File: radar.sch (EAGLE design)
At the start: 9 parts, among them J1 APP_2POS_CONFIG12V_HORIZ, U1 OKI-78SR-3.3/1.5-W36HC, U2 OKI-78SR-5/1.5-W36HC

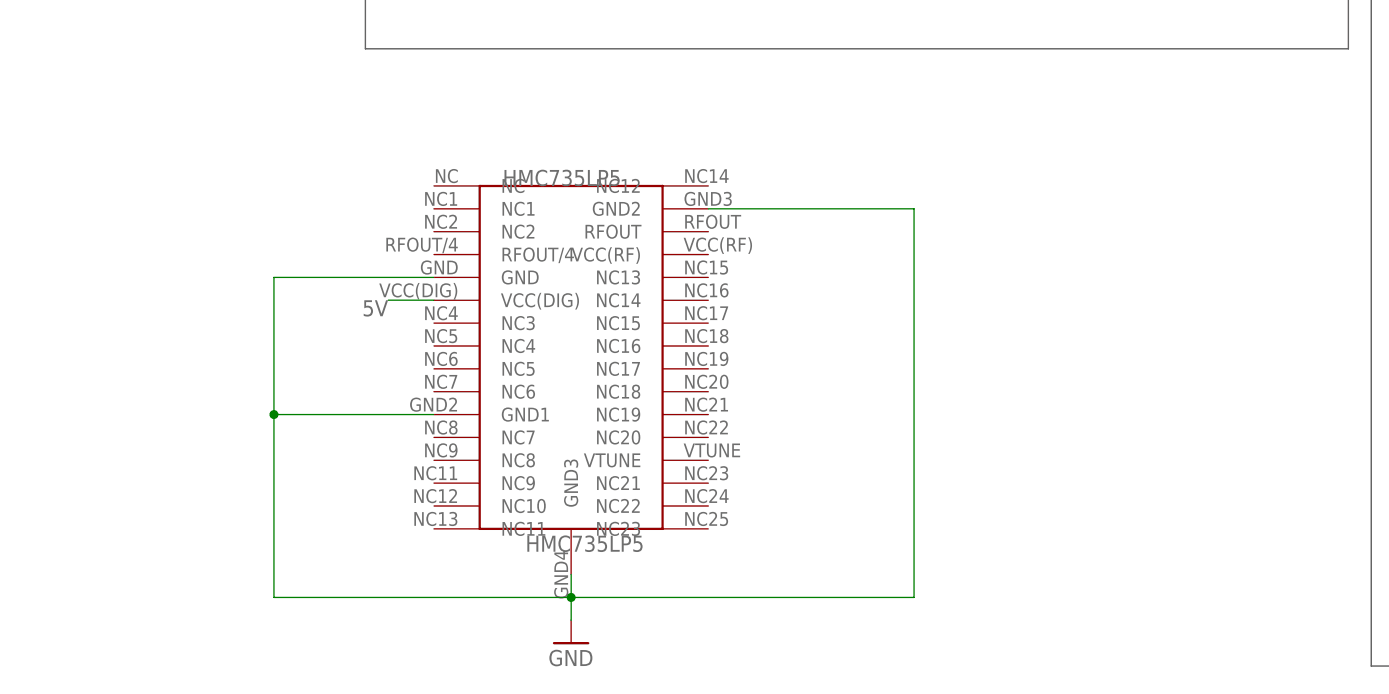
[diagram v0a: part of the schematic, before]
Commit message: Created PLL library and added it to schematic
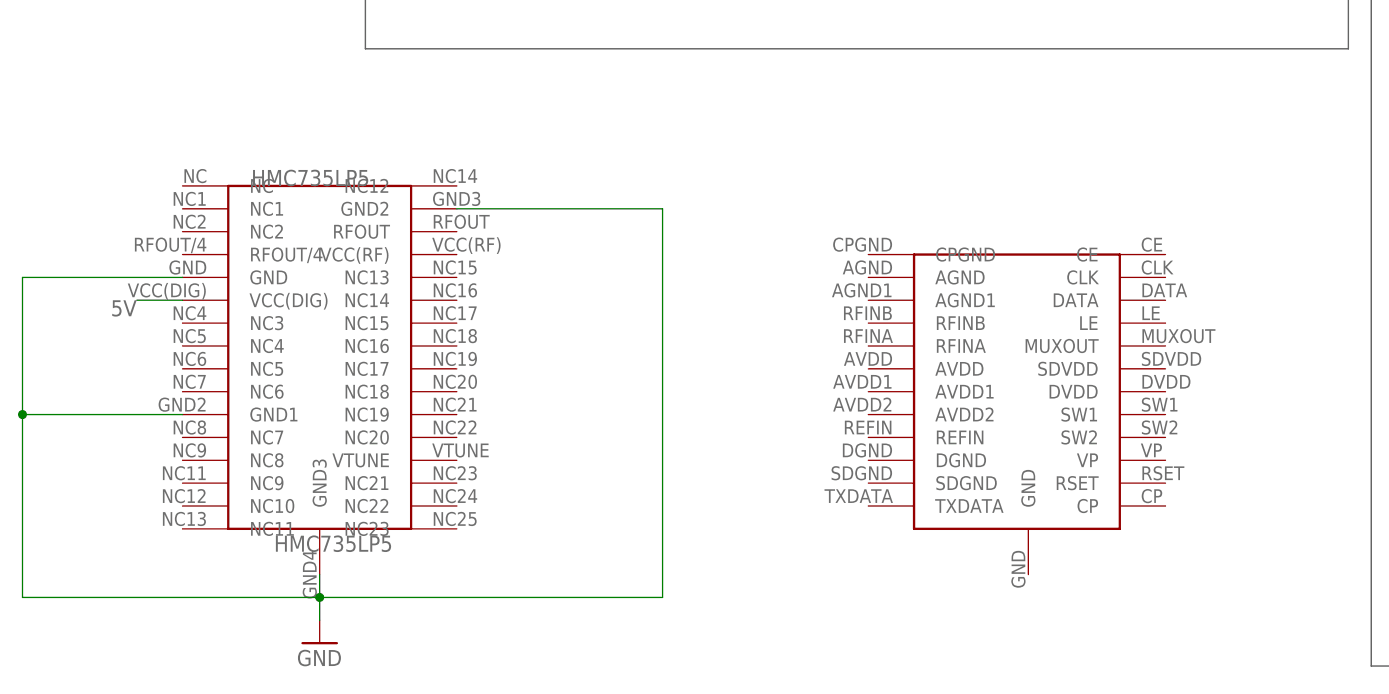
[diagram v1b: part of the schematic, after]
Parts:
- added U$3: ADF4169, ADF4169:ADF4169
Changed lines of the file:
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@@
 <part name="GND4" library="supply1" deviceset="GND" device=""/>
 <part name="U$2" library="HMC735LP5" deviceset="HMC735LP5" device=""/>
+<part name="U$3" library="ADF4169" deviceset="ADF4169" device=""/>
 </parts>
 <sheets>
@@
 <instance part="GND2" gate="1" x="0" y="109.22"/>
 <instance part="GND3" gate="1" x="43.18" y="109.22"/>
-<instance part="GND4" gate="1" x="-2.54" y="30.48"/>
-<instance part="U$2" gate="G$1" x="-2.54" y="68.58"/>
+<instance part="GND4" gate="1" x="-30.48" y="30.48"/>
+<instance part="U$2" gate="G$1" x="-30.48" y="68.58"/>
+<instance part="U$3" gate="G$1" x="45.72" y="55.88"/>
 </instances>
 <busses>
@@
 <pinref part="GND4" gate="1" pin="GND"/>
 <pinref part="U$2" gate="G$1" pin="GND3"/>
-<wire x1="-2.54" y1="33.02" x2="-2.54" y2="35.56" width="0.1524" layer="91"/>
+<wire x1="-30.48" y1="33.02" x2="-30.48" y2="35.56" width="0.1524" layer="91"/>
 <pinref part="U$2" gate="G$1" pin="GND"/>
-<wire x1="-2.54" y1="35.56" x2="-2.54" y2="38.1" width="0.1524" layer="91"/>
-<wire x1="-17.78" y1="71.12" x2="-35.56" y2="71.12" width="0.1524" layer="91"/>
-<wire x1="-35.56" y1="71.12" x2="-35.56" y2="55.88" width="0.1524" layer="91"/>
-<wire x1="-35.56" y1="55.88" x2="-35.56" y2="35.56" width="0.1524" layer="91"/>
-<wire x1="-35.56" y1="35.56" x2="-2.54" y2="35.56" width="0.1524" layer="91"/>
-<junction x="-2.54" y="35.56"/>
+<wire x1="-30.48" y1="35.56" x2="-30.48" y2="38.1" width="0.1524" layer="91"/>
+<wire x1="-45.72" y1="71.12" x2="-63.5" y2="71.12" width="0.1524" layer="91"/>
+<wire x1="-63.5" y1="71.12" x2="-63.5" y2="55.88" width="0.1524" layer="91"/>
+<wire x1="-63.5" y1="55.88" x2="-63.5" y2="35.56" width="0.1524" layer="91"/>
+<wire x1="-63.5" y1="35.56" x2="-30.48" y2="35.56" width="0.1524" layer="91"/>
+<junction x="-30.48" y="35.56"/>
 <pinref part="U$2" gate="G$1" pin="GND1"/>
-<wire x1="-17.78" y1="55.88" x2="-35.56" y2="55.88" width="0.1524" layer="91"/>
-<junction x="-35.56" y="55.88"/>
+<wire x1="-45.72" y1="55.88" x2="-63.5" y2="55.88" width="0.1524" layer="91"/>
+<junction x="-63.5" y="55.88"/>
 <pinref part="U$2" gate="G$1" pin="GND2"/>
-<wire x1="12.7" y1="78.74" x2="35.56" y2="78.74" width="0.1524" layer="91"/>
-<wire x1="35.56" y1="78.74" x2="35.56" y2="35.56" width="0.1524" layer="91"/>
-<wire x1="35.56" y1="35.56" x2="-2.54" y2="35.56" width="0.1524" layer="91"/>
+<wire x1="-15.24" y1="78.74" x2="7.62" y2="78.74" width="0.1524" layer="91"/>
+<wire x1="7.62" y1="78.74" x2="7.62" y2="35.56" width="0.1524" layer="91"/>
+<wire x1="7.62" y1="35.56" x2="-30.48" y2="35.56" width="0.1524" layer="91"/>
 </segment>
 </net>
@@
 <segment>
 <pinref part="U$2" gate="G$1" pin="VCC(DIG)"/>
-<wire x1="-17.78" y1="68.58" x2="-22.86" y2="68.58" width="0.1524" layer="91"/>
-<label x="-22.86" y="68.58" size="1.778" layer="95" rot="R180"/>
+<wire x1="-45.72" y1="68.58" x2="-50.8" y2="68.58" width="0.1524" layer="91"/>
+<label x="-50.8" y="68.58" size="1.778" layer="95" rot="R180"/>
 </segment>
 </net>

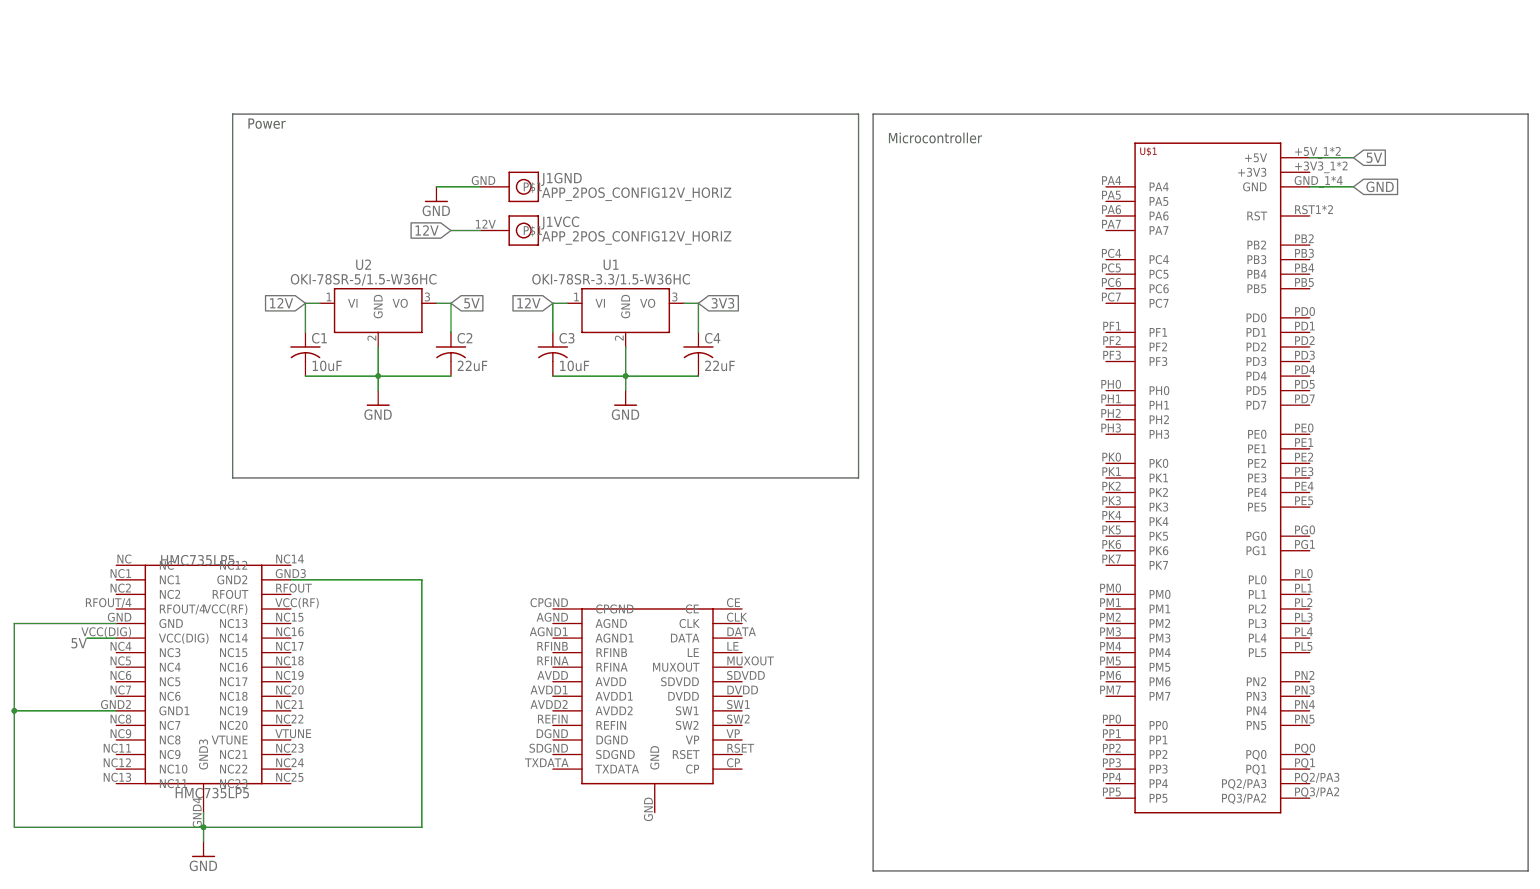
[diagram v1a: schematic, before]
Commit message: Started board layout
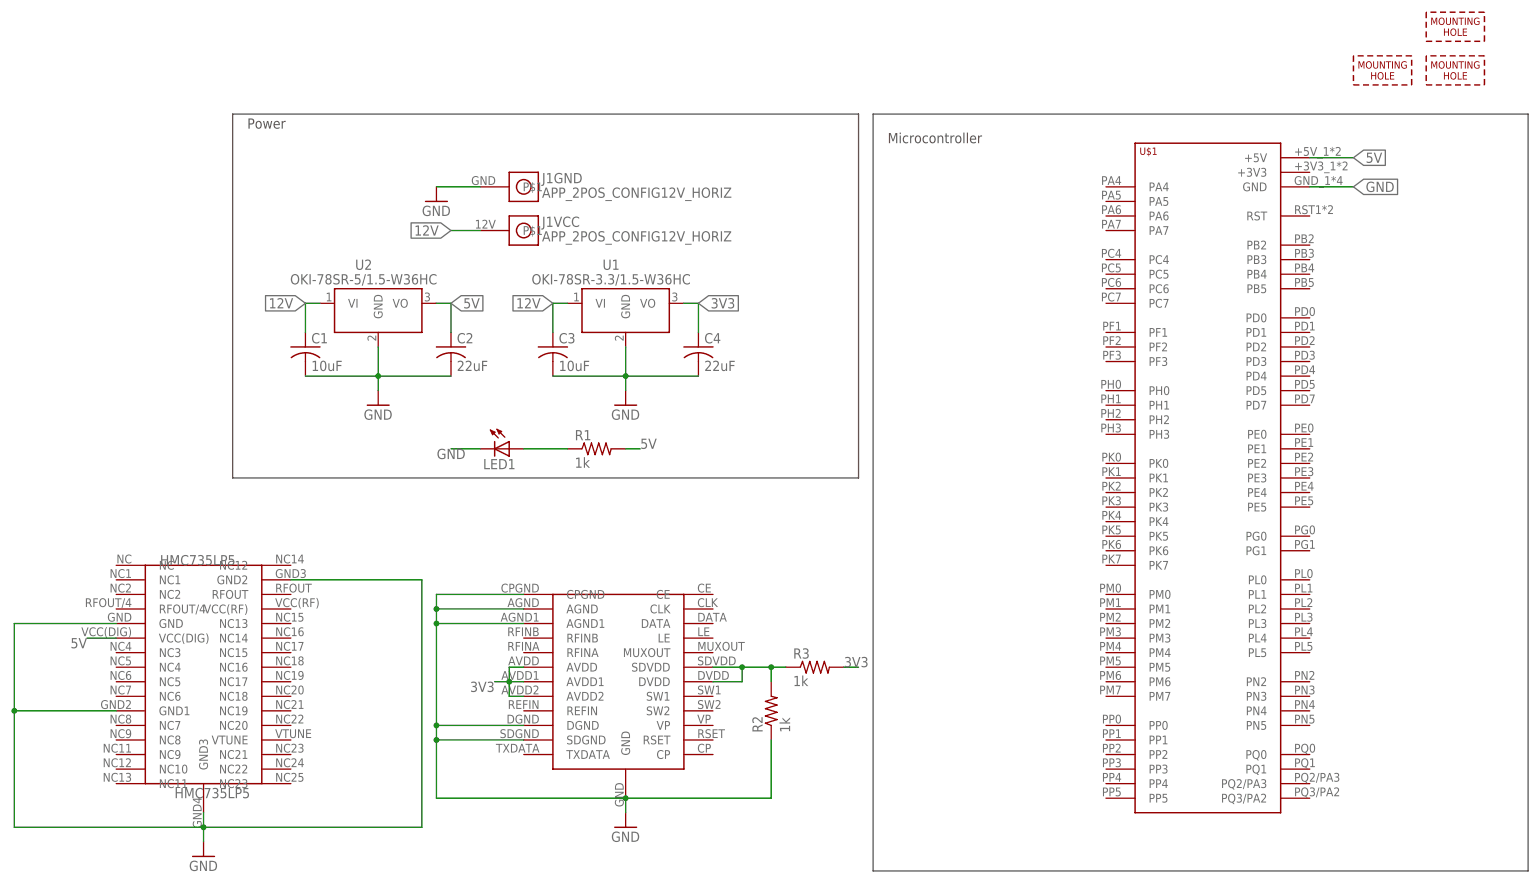
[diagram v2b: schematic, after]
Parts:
- added H1, H2, H3: MOUNTING_HOLE#6, MRDT-Hardware:MOUNTING_HOLE#6
- added LED1: (no value), led:LEDCHIP-LED0805
- added R1, R2, R3: 1k, rcl:R-US_M0805
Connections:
- new net N$1: LED1.A, R1.1
- new net N$2: R2.2, R3.1, U$3.DVDD, U$3.SDVDD
- net 3V3: now also R3.2, U$3.AVDD, U$3.AVDD1, U$3.AVDD2
- net 5V: now also R1.2
- net GND: now also LED1.C, R2.1, U$3.AGND, U$3.AGND1, U$3.CPGND, U$3.DGND, U$3.GND, U$3.SDGND
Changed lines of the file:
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@@
 <part name="U$2" library="HMC735LP5" deviceset="HMC735LP5" device=""/>
 <part name="U$3" library="ADF4169" deviceset="ADF4169" device=""/>
+<part name="LED1" library="led" deviceset="LED" device="CHIP-LED0805"/>
+<part name="R1" library="rcl" deviceset="R-US_" device="M0805" value="1k"/>
+<part name="GND5" library="supply1" deviceset="GND" device=""/>
+<part name="R2" library="rcl" deviceset="R-US_" device="M0805" value="1k"/>
+<part name="R3" library="rcl" deviceset="R-US_" device="M0805" value="1k"/>
+<part name="H1" library="MRDT-Hardware" deviceset="MOUNTING_HOLE" device="#6"/>
+<part name="H2" library="MRDT-Hardware" deviceset="MOUNTING_HOLE" device="#6"/>
+<part name="H3" library="MRDT-Hardware" deviceset="MOUNTING_HOLE" device="#6"/>
 </parts>
 <sheets>
@@
 <instance part="GND4" gate="1" x="-30.48" y="30.48"/>
 <instance part="U$2" gate="G$1" x="-30.48" y="68.58"/>
-<instance part="U$3" gate="G$1" x="45.72" y="55.88"/>
+<instance part="U$3" gate="G$1" x="40.64" y="58.42"/>
+<instance part="LED1" gate="G$1" x="22.86" y="101.6" rot="R270"/>
+<instance part="R1" gate="G$1" x="38.1" y="101.6"/>
+<instance part="GND5" gate="1" x="43.18" y="35.56"/>
+<instance part="R2" gate="G$1" x="68.58" y="55.88" rot="R90"/>
+<instance part="R3" gate="G$1" x="76.2" y="63.5"/>
+<instance part="H1" gate="G$1" x="182.88" y="165.1"/>
+<instance part="H2" gate="G$1" x="182.88" y="172.72"/>
+<instance part="H3" gate="G$1" x="170.18" y="165.1"/>
 </instances>
 <busses>
@@
 <wire x1="7.62" y1="35.56" x2="-30.48" y2="35.56" width="0.1524" layer="91"/>
 </segment>
+<segment>
+<pinref part="LED1" gate="G$1" pin="C"/>
+<wire x1="17.78" y1="101.6" x2="12.7" y2="101.6" width="0.1524" layer="91"/>
+<label x="15.24" y="101.6" size="1.778" layer="95" rot="R180"/>
+</segment>
+<segment>
+<pinref part="U$3" gate="G$1" pin="CPGND"/>
+<wire x1="25.4" y1="76.2" x2="10.16" y2="76.2" width="0.1524" layer="91"/>
+<wire x1="10.16" y1="76.2" x2="10.16" y2="73.66" width="0.1524" layer="91"/>
+<pinref part="U$3" gate="G$1" pin="GND"/>
+<wire x1="10.16" y1="73.66" x2="10.16" y2="71.12" width="0.1524" layer="91"/>
+<wire x1="10.16" y1="71.12" x2="10.16" y2="53.34" width="0.1524" layer="91"/>
+<wire x1="10.16" y1="53.34" x2="10.16" y2="50.8" width="0.1524" layer="91"/>
+<wire x1="10.16" y1="50.8" x2="10.16" y2="40.64" width="0.1524" layer="91"/>
+<wire x1="10.16" y1="40.64" x2="43.18" y2="40.64" width="0.1524" layer="91"/>
+<pinref part="U$3" gate="G$1" pin="AGND"/>
+<wire x1="25.4" y1="73.66" x2="10.16" y2="73.66" width="0.1524" layer="91"/>
+<junction x="10.16" y="73.66"/>
+<pinref part="U$3" gate="G$1" pin="AGND1"/>
+<wire x1="25.4" y1="71.12" x2="10.16" y2="71.12" width="0.1524" layer="91"/>
+<junction x="10.16" y="71.12"/>
+<pinref part="U$3" gate="G$1" pin="DGND"/>
+<wire x1="25.4" y1="53.34" x2="10.16" y2="53.34" width="0.1524" layer="91"/>
+<junction x="10.16" y="53.34"/>
+<pinref part="U$3" gate="G$1" pin="SDGND"/>
+<wire x1="25.4" y1="50.8" x2="10.16" y2="50.8" width="0.1524" layer="91"/>
+<junction x="10.16" y="50.8"/>
+<pinref part="GND5" gate="1" pin="GND"/>
+<wire x1="43.18" y1="40.64" x2="43.18" y2="38.1" width="0.1524" layer="91"/>
+<junction x="43.18" y="40.64"/>
+<pinref part="R2" gate="G$1" pin="1"/>
+<wire x1="68.58" y1="50.8" x2="68.58" y2="40.64" width="0.1524" layer="91"/>
+<wire x1="68.58" y1="40.64" x2="43.18" y2="40.64" width="0.1524" layer="91"/>
+</segment>
 </net>
 <net name="5V" class="0">
@@
 <label x="-50.8" y="68.58" size="1.778" layer="95" rot="R180"/>
 </segment>
+<segment>
+<pinref part="R1" gate="G$1" pin="2"/>
+<wire x1="43.18" y1="101.6" x2="45.72" y2="101.6" width="0.1524" layer="91"/>
+<label x="45.72" y="101.6" size="1.778" layer="95"/>
+</segment>
 </net>
 <net name="3V3" class="0">
@@
 <label x="55.88" y="127" size="1.778" layer="95" xref="yes"/>
 </segment>
+<segment>
+<pinref part="U$3" gate="G$1" pin="AVDD"/>
+<wire x1="25.4" y1="63.5" x2="22.86" y2="63.5" width="0.1524" layer="91"/>
+<wire x1="22.86" y1="63.5" x2="22.86" y2="60.96" width="0.1524" layer="91"/>
+<pinref part="U$3" gate="G$1" pin="AVDD1"/>
+<wire x1="22.86" y1="60.96" x2="25.4" y2="60.96" width="0.1524" layer="91"/>
+<wire x1="22.86" y1="60.96" x2="22.86" y2="58.42" width="0.1524" layer="91"/>
+<junction x="22.86" y="60.96"/>
+<pinref part="U$3" gate="G$1" pin="AVDD2"/>
+<wire x1="22.86" y1="58.42" x2="25.4" y2="58.42" width="0.1524" layer="91"/>
+<wire x1="22.86" y1="60.96" x2="20.32" y2="60.96" width="0.1524" layer="91"/>
+<label x="20.32" y="60.96" size="1.778" layer="95" rot="R180"/>
+</segment>
+<segment>
+<pinref part="R3" gate="G$1" pin="2"/>
+<wire x1="81.28" y1="63.5" x2="83.82" y2="63.5" width="0.1524" layer="91"/>
+<label x="81.28" y="63.5" size="1.778" layer="95"/>
+</segment>
 </net>
 <net name="12V" class="0">
@@
 </segment>
 </net>
+<net name="N$1" class="0">
+<segment>
+<pinref part="R1" gate="G$1" pin="1"/>
+<pinref part="LED1" gate="G$1" pin="A"/>
+<wire x1="33.02" y1="101.6" x2="25.4" y2="101.6" width="0.1524" layer="91"/>
+</segment>
+</net>
+<net name="N$2" class="0">
+<segment>
+<pinref part="U$3" gate="G$1" pin="SDVDD"/>
+<wire x1="58.42" y1="63.5" x2="63.5" y2="63.5" width="0.1524" layer="91"/>
+<wire x1="63.5" y1="63.5" x2="63.5" y2="60.96" width="0.1524" layer="91"/>
+<pinref part="U$3" gate="G$1" pin="DVDD"/>
+<wire x1="63.5" y1="60.96" x2="58.42" y2="60.96" width="0.1524" layer="91"/>
+<wire x1="63.5" y1="63.5" x2="68.58" y2="63.5" width="0.1524" layer="91"/>
+<junction x="63.5" y="63.5"/>
+<pinref part="R2" gate="G$1" pin="2"/>
+<wire x1="68.58" y1="60.96" x2="68.58" y2="63.5" width="0.1524" layer="91"/>
+<pinref part="R3" gate="G$1" pin="1"/>
+<wire x1="68.58" y1="63.5" x2="71.12" y2="63.5" width="0.1524" layer="91"/>
+<junction x="68.58" y="63.5"/>
+</segment>
+</net>
